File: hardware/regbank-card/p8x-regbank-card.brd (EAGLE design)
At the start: 160 x 100 mm, 95 parts, among them J1 FABC96R, U1 P0 L0, U10 P2 L1, U11 P2 H0, U12 P2 H1, U13 P3 L0, U14 P3 L1, U15 P3 H0, U16 P3 H1, U17 PTR SEL 0, U18 PTR SEL 1, U19 PTR SEL 2, U2 P0 L1, U20 PTR SEL 3, U21 PTR SEL 4, U22 PTR SEL 5, U23 PTR SEL 6, U24 PTR SEL 7, U25 ADDR LO, U26 ADDR HI, U27 RDBK LO, U28 RDBK HI, U29 RDBK OUT, U3 P0 H0, U30 DLD DEC, U31 DOE DEC, U32 LOAD DEC, U33 SEL DEC, U34 74HCT02, U35 74HCT14, U36 ZERO P0, U37 74HCT08, U38 74HCT08, U39 CNT DEC, U4 P0 H1, U40 74HCT32, U41 PT LO, U42 PT HI, U43 PT SEL LO, U44 PT SEL HI, U5 P1 L0, U6 P1 L1, U7 P1 H0, U8 P1 H1, U9 P2 L0

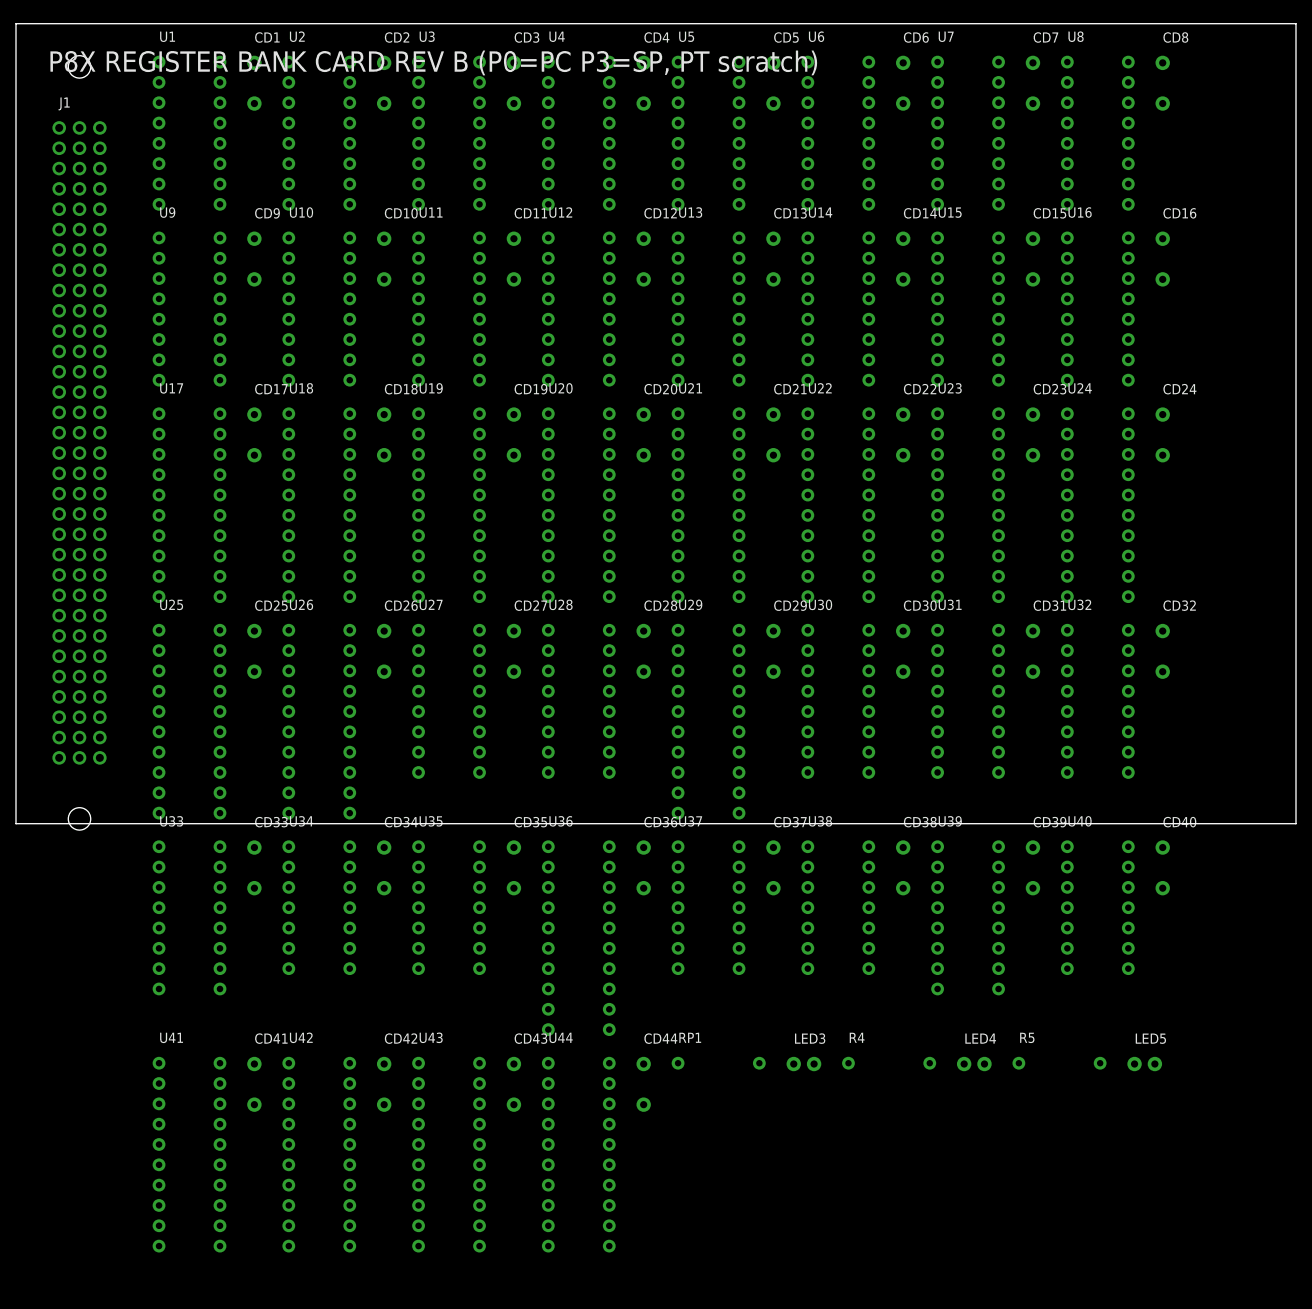
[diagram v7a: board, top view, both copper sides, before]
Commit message: feat(generators): faithful Eagle/Fusion output (values, layers, smashed parts)
Make the generated .sch/.brd match how Eagle itself writes files, so Fusion
displays everything correctly (was mis-mapping names/values to scratch layers):

- devicesets get uservalue="yes" so the `value` field is honored at all (it was
  silently ignored before — no card's value ever displayed)
- emit the COMPLETE standard Eagle layer table (62 layers) in every drawing, so
  Fusion has nothing to remap on import
- board elements are now smashed="yes" with explicit NAME (tNames/25) and VALUE
  (tValues/27) attributes — refdes + part number show reliably
- add std <attributes>/<variantdefs> board sections + board-package >VALUE silk
- schematic: `value` holds the orderable part number (>VALUE + BOM); the logical
  function is placed as text near each chip via a new card() `labels` arg
- write_brd gains outline_only and unplaced modes (parts off-board + ratsnest);
  card() exposes brd_outline_only / brd_unplaced

Proven on the LED card (part numbers + function labels + an unplaced 4-layer
board). The other cards get the structural fixes now; rolling the part-number/
labels convention across them is the next step. All 8 boards validate (0 errors).

Co-Authored-By: Claude Opus 4.8 <noreply@anthropic.com>
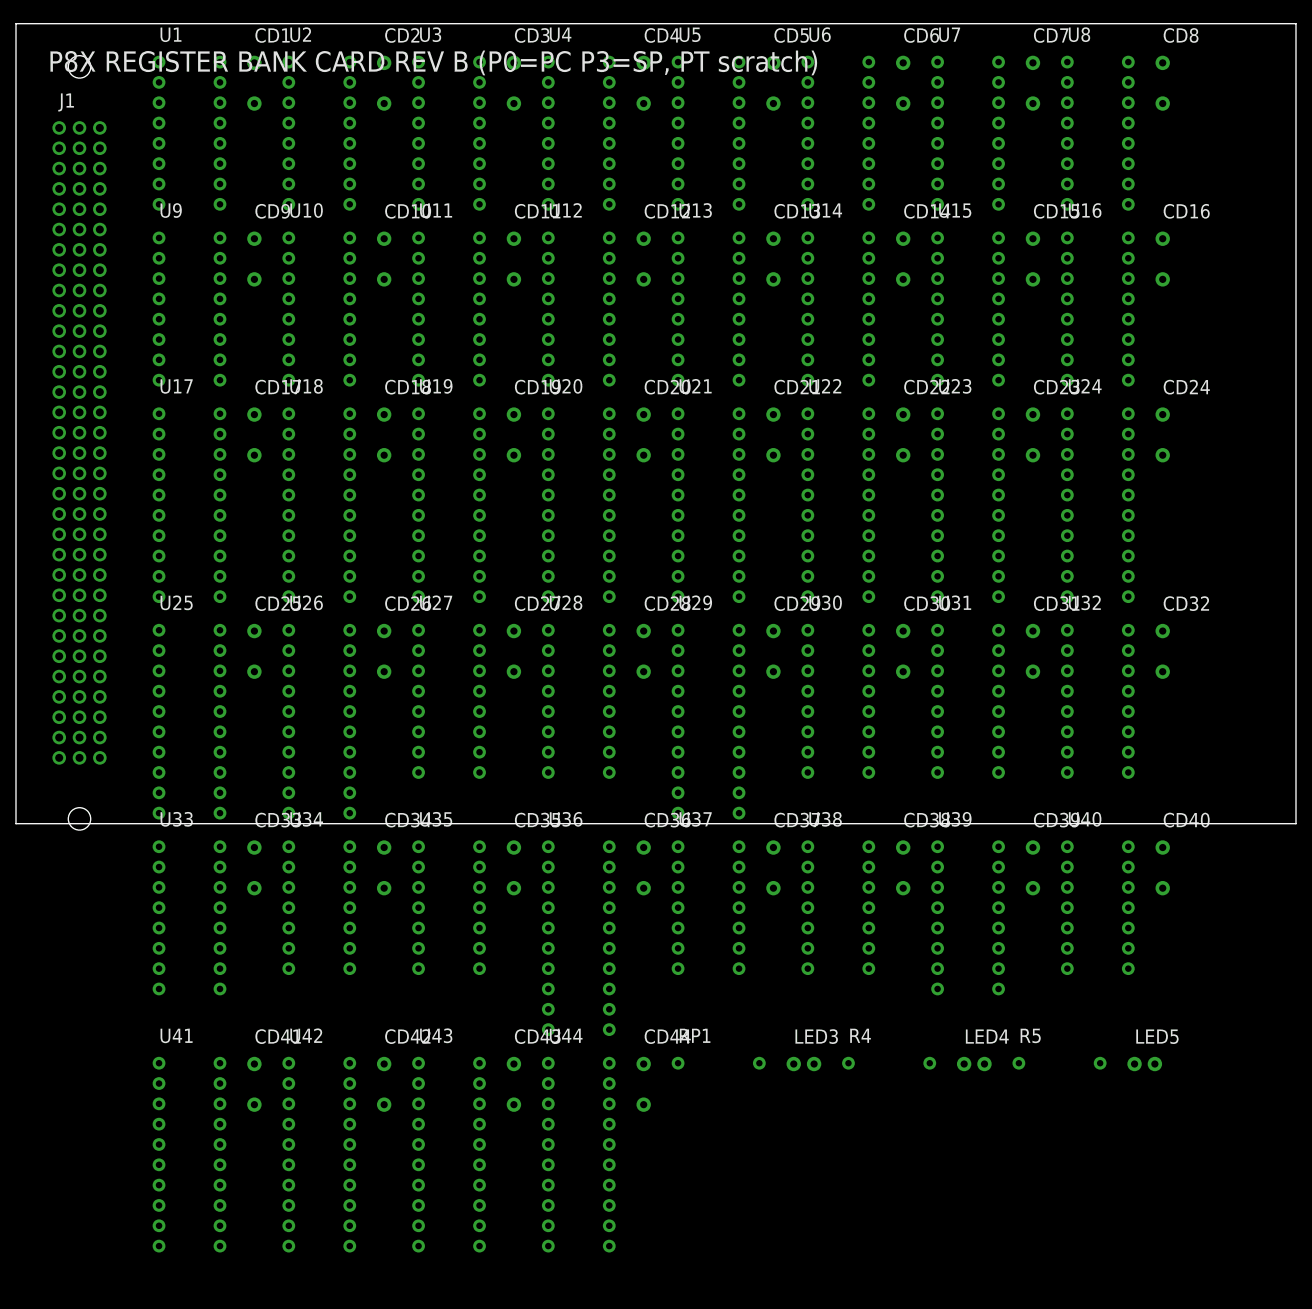
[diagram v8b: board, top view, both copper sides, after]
